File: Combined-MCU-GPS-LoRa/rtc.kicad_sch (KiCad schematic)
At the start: 0 parts

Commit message: Added Readme
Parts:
- added U2: X1B000301000200, PARTS:OSC-SMD_10P-L3.2-W2.5-BL-1, symbol PARTS:X1B000301000200
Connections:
- new net GND: U2.9 (GND)
- new net INT: U2.10 (~{INT})
- new net SCL: U2.5 (SCL)
- new net SDA: U2.7 (SDA)
- new net VBAT: U2.3 (VBAT)
- new net VCC_RTC: U2.2 (VDD)
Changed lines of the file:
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@@
 (kicad_sch (version 20230121) (generator eeschema)
   (paper "A4")
+  (hierarchical_label "SDA" (shape input) (at 156.21 91.44 0) (fields_autoplaced)
+    (effects (font (size 1.27 1.27)) (justify left))
+  )
+  (hierarchical_label "SCL" (shape input) (at 133.35 93.98 180) (fields_autoplaced)
+    (effects (font (size 1.27 1.27)) (justify right))
+  )
+  (hierarchical_label "VCC_RTC" (shape input) (at 133.35 86.36 180) (fields_autoplaced)
+    (effects (font (size 1.27 1.27)) (justify right))
+  )
+  (hierarchical_label "INT" (shape input) (at 156.21 83.82 0) (fields_autoplaced)
+    (effects (font (size 1.27 1.27)) (justify left))
+  )
+  (hierarchical_label "VBAT" (shape input) (at 133.35 88.9 180) (fields_autoplaced)
+    (effects (font (size 1.27 1.27)) (justify right))
+  )
+  (symbol (lib_id "PARTS:X1B000301000200") (at 144.78 88.9 0) (unit 1)
+    (in_bom yes) (on_board yes) (dnp no) (fields_autoplaced)
+    (property "Reference" "U2" (at 144.78 76.2 0)
+      (effects (font (size 1.27 1.27)))
+    )
+    (property "Value" "X1B000301000200" (at 144.78 78.74 0)
+      (effects (font (size 1.27 1.27)))
+    )
+    (property "Footprint" "PARTS:OSC-SMD_10P-L3.2-W2.5-BL-1" (at 144.78 101.6 0)
+      (effects (font (size 1.27 1.27)) hide)
+    )
+    (property "Datasheet" "" (at 144.78 88.9 0)
+      (effects (font (size 1.27 1.27)) hide)
+    )
+    (property "LCSC Part" "C7528386" (at 144.78 104.14 0)
+      (effects (font (size 1.27 1.27)) hide)
+    )
+    (pin "1")
+    (pin "10")
+    (pin "2")
+    (pin "3")
+    (pin "4")
+    (pin "5")
+    (pin "6")
+    (pin "7")
+    (pin "8")
+    (pin "9")
+    (instances
+      (project "Combined-MCU-GPS-LoRa"
+        (path "/a0175fec-7c81-4d4b-9fe1-21009e5acfd6/4f948912-26aa-4814-8f55-73b5add1c17d"
+          (reference "U2") (unit 1)
+        )
+      )
+    )
+  )
+  (symbol (lib_id "power:GND") (at 156.21 86.36 90) (unit 1)
+    (in_bom yes) (on_board yes) (dnp no) (fields_autoplaced)
+    (property "Reference" "#PWR06" (at 162.56 86.36 0)
+      (effects (font (size 1.27 1.27)) hide)
+    )
+    (property "Value" "GND" (at 160.02 86.36 90)
+      (effects (font (size 1.27 1.27)) (justify right))
+    )
+    (property "Footprint" "" (at 156.21 86.36 0)
+      (effects (font (size 1.27 1.27)) hide)
+    )
+    (property "Datasheet" "" (at 156.21 86.36 0)
+      (effects (font (size 1.27 1.27)) hide)
+    )
+    (pin "1")
+    (instances
+      (project "Combined-MCU-GPS-LoRa"
+        (path "/a0175fec-7c81-4d4b-9fe1-21009e5acfd6/4f948912-26aa-4814-8f55-73b5add1c17d"
+          (reference "#PWR06") (unit 1)
+        )
+      )
+    )
+  )
 )

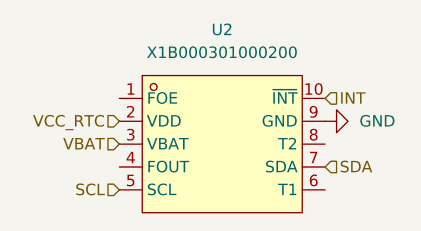
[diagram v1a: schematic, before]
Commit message: I think I have the schematic done.
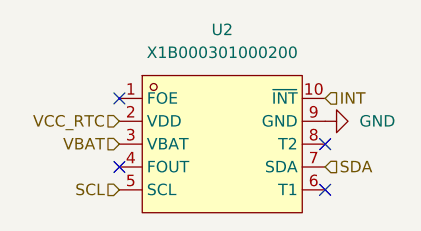
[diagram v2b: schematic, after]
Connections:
- no-connect marks 0 -> 4
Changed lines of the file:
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@@
 (kicad_sch (version 20230121) (generator eeschema)
   (paper "A4")
+  (no_connect (at 133.35 91.44))
+  (no_connect (at 156.21 88.9))
+  (no_connect (at 156.21 93.98))
+  (no_connect (at 133.35 83.82))
   (hierarchical_label "SDA" (shape input) (at 156.21 91.44 0) (fields_autoplaced)
     (effects (font (size 1.27 1.27)) (justify left))
